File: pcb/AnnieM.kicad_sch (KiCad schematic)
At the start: 24 parts, among them J1 NRG200P, J2 NRG400, J3 SOLAR, U1 LMT86, U3 LM393

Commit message: added pull up to schematic
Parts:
- added R10: 100K, Resistor_SMD:R_0603_1608Metric, symbol Device:R
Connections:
- net VCC: now also R10.2
- net at C9.2, D1.1 (K), U3.1: now also R10.1
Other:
- moved on the sheet: D1
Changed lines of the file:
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@@
   (junction (at 156.21 82.55) (diameter 0) (color 0 0 0 0)
+  )
+  (junction (at 195.58 74.93) (diameter 0) (color 0 0 0 0)
   )
   (junction (at 133.35 109.22) (diameter 0) (color 0 0 0 0)
@@
     (stroke (width 0) (type default) (color 0 0 0 0))
   )
+  (wire (pts (xy 195.58 74.93) (xy 196.85 74.93))
+    (stroke (width 0) (type default) (color 0 0 0 0))
+  )
   (wire (pts (xy 149.86 74.93) (xy 156.21 74.93))
     (stroke (width 0) (type default) (color 0 0 0 0))
   )
-  (wire (pts (xy 199.39 74.93) (xy 201.93 74.93))
+  (wire (pts (xy 204.47 74.93) (xy 207.01 74.93))
     (stroke (width 0) (type default) (color 0 0 0 0))
   )
@@
     (stroke (width 0) (type default) (color 0 0 0 0))
   )
+  (wire (pts (xy 195.58 74.93) (xy 195.58 78.74))
+    (stroke (width 0) (type default) (color 0 0 0 0))
+  )
   (wire (pts (xy 146.05 36.83) (xy 154.94 36.83))
     (stroke (width 0) (type default) (color 0 0 0 0))
@@
     (stroke (width 0) (type default) (color 0 0 0 0))
   )
-  (wire (pts (xy 187.96 74.93) (xy 191.77 74.93))
+  (wire (pts (xy 187.96 74.93) (xy 195.58 74.93))
     (stroke (width 0) (type default) (color 0 0 0 0))
   )
@@
     )
   )
-  (global_label "SPEED" (shape output) (at 201.93 74.93 0) (fields_autoplaced)
+  (global_label "SPEED" (shape output) (at 207.01 74.93 0) (fields_autoplaced)
     (effects (font (size 1.27 1.27)) (justify left))
-    (property "Intersheet References" "${INTERSHEET_REFS}" (id 0) (at -11.43 29.21 0)
+    (property "Intersheet References" "${INTERSHEET_REFS}" (id 0) (at -6.35 29.21 0)
       (effects (font (size 1.27 1.27)) hide)
     )
@@
     )
     (property "Datasheet" "" (id 3) (at 240.03 69.85 0)
+      (effects (font (size 1.27 1.27)) hide)
+    )
+    (pin "1")
+  )
+  (symbol (lib_id "power:VCC") (at 195.58 86.36 180) (unit 1)
+    (in_bom yes) (on_board yes)
+    (property "Reference" "#PWR02" (id 0) (at 195.58 82.55 0)
+      (effects (font (size 1.27 1.27)) hide)
+    )
+    (property "Value" "VCC" (id 1) (at 195.58 91.44 0))
+    (property "Footprint" "" (id 2) (at 195.58 86.36 0)
+      (effects (font (size 1.27 1.27)) hide)
+    )
+    (property "Datasheet" "" (id 3) (at 195.58 86.36 0)
       (effects (font (size 1.27 1.27)) hide)
     )
@@
     (pin "1")
   )
-  (symbol (lib_id "Diode:1N914") (at 195.58 74.93 0) (unit 1)
+  (symbol (lib_id "Diode:1N914") (at 200.66 74.93 0) (unit 1)
     (in_bom yes) (on_board yes) (fields_autoplaced)
-    (property "Reference" "D1" (id 0) (at 195.58 68.58 0))
-    (property "Value" "1N914" (id 1) (at 195.58 71.12 0))
-    (property "Footprint" "Diode_THT:D_DO-35_SOD27_P7.62mm_Horizontal" (id 2) (at 195.58 79.375 0)
-      (effects (font (size 1.27 1.27)) hide)
-    )
-    (property "Datasheet" "http://www.vishay.com/docs/85622/1n914.pdf" (id 3) (at 195.58 74.93 0)
+    (property "Reference" "D1" (id 0) (at 200.66 68.58 0))
+    (property "Value" "1N914" (id 1) (at 200.66 71.12 0))
+    (property "Footprint" "Diode_THT:D_DO-35_SOD27_P7.62mm_Horizontal" (id 2) (at 200.66 79.375 0)
+      (effects (font (size 1.27 1.27)) hide)
+    )
+    (property "Datasheet" "http://www.vishay.com/docs/85622/1n914.pdf" (id 3) (at 200.66 74.93 0)
       (effects (font (size 1.27 1.27)) hide)
     )
@@
     )
     (pin "1")
+  )
+  (symbol (lib_id "Device:R") (at 195.58 82.55 0) (unit 1)
+    (in_bom yes) (on_board yes)
+    (property "Reference" "R10" (id 0) (at 193.04 82.55 90))
+    (property "Value" "100K" (id 1) (at 195.58 82.55 90))
+    (property "Footprint" "Resistor_SMD:R_0603_1608Metric" (id 2) (at 193.802 82.55 90)
+      (effects (font (size 1.27 1.27)) hide)
+    )
+    (property "Datasheet" "~" (id 3) (at 195.58 82.55 0)
+      (effects (font (size 1.27 1.27)) hide)
+    )
+    (pin "1")
+    (pin "2")
   )
   (symbol (lib_id "Device:C") (at 146.05 40.64 180) (unit 1)
@@
       (reference "#PWR01") (unit 1) (value "+10V") (footprint "")
     )
+    (path "/53498bcf-60b7-4c8d-9f37-8e4f9e563988"
+      (reference "#PWR02") (unit 1) (value "VCC") (footprint "")
+    )
     (path "/ba6c0b9c-fd1d-41af-a893-efc60d38ab3c"
       (reference "#PWR03") (unit 1) (value "+10V") (footprint "")
@@
       (reference "R9") (unit 1) (value "10K") (footprint "Resistor_SMD:R_0603_1608Metric")
     )
+    (path "/bbc3e4fe-b40f-4f24-b198-21d5f04f0ba7"
+      (reference "R10") (unit 1) (value "100K") (footprint "Resistor_SMD:R_0603_1608Metric")
+    )
     (path "/e0207eaa-3301-4772-a50e-fb4c3ab37719"

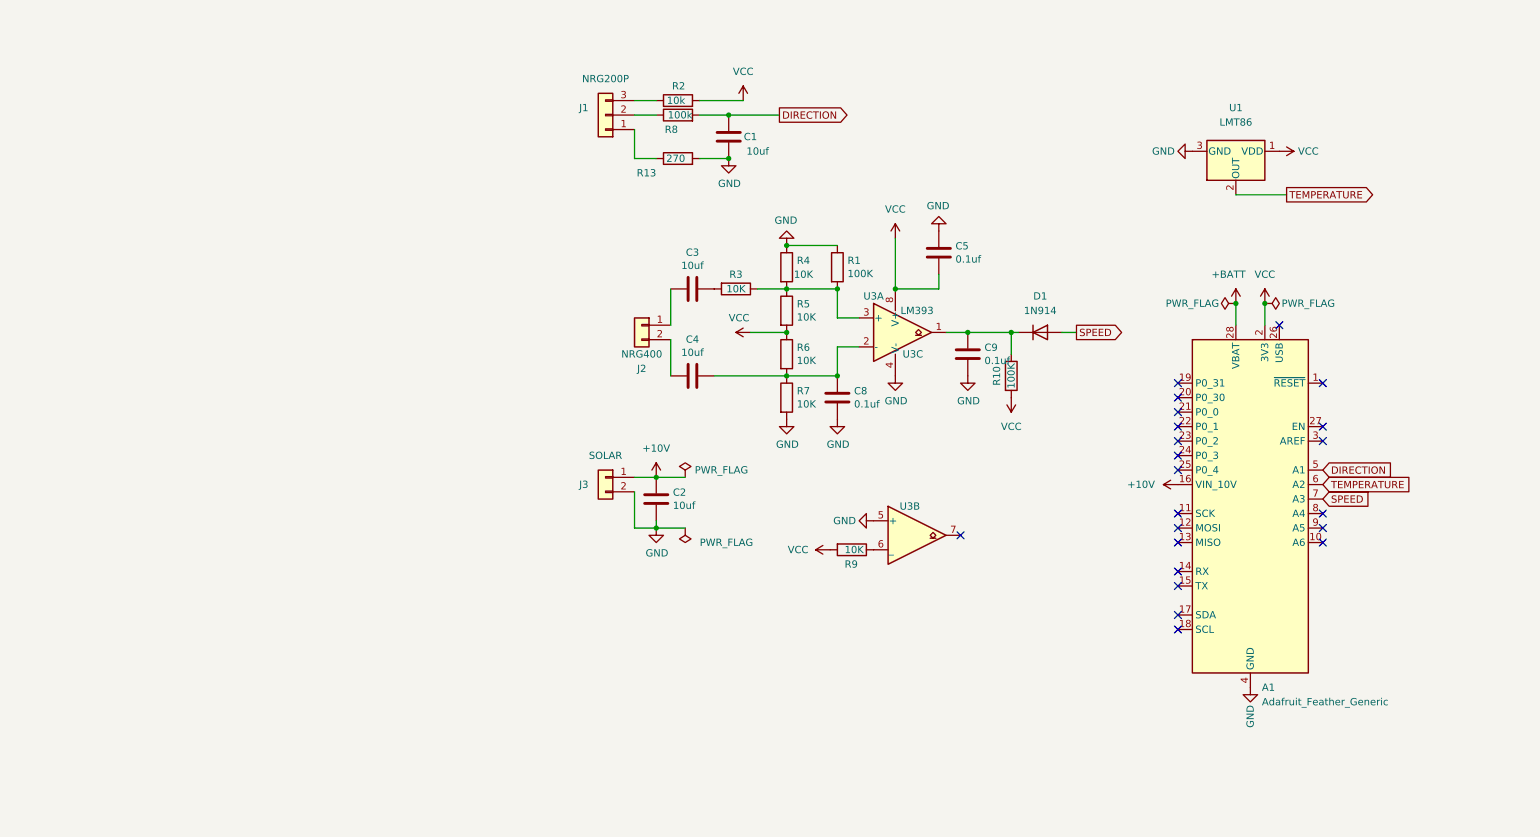
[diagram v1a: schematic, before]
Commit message: Restarted pcb layout, added bme866 and Arducam 5MP
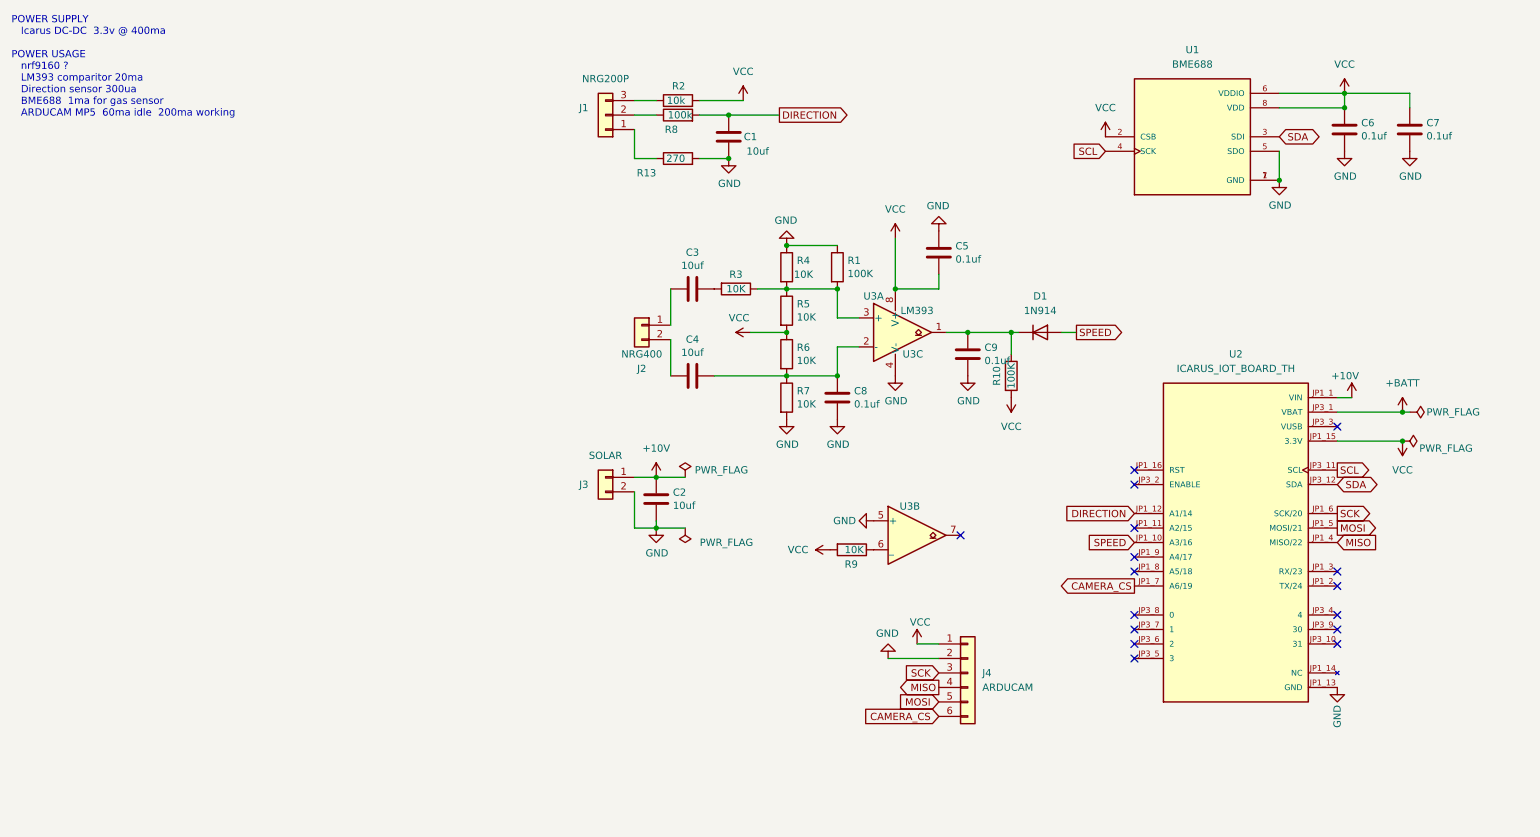
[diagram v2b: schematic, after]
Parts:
- removed A1: Adafruit_Feather_Generic, Module:Adafruit_Feather, symbol MCU_Module:Adafruit_Feather_Generic
- removed U1: LMT86, Package_TO_SOT_THT:TO-92_Inline, symbol Regulator_Linear:L78L18_TO92
- added C6, C7: 0.1uf, Capacitor_SMD:C_0603_1608Metric, symbol Device:C
- added J4: ARDUCAM, Connector_PinHeader_2.54mm:PinHeader_1x06_P2.54mm_Vertical, symbol Connector_Generic:Conn_01x06
- added U1: BME688, BME688:IC_BME688, symbol BME688:BME688
- added U2: ICARUS_IOT_BOARD_TH, ICARUS_IOT_BOARD_TH:MODULE_ICARUS_IOT_BOARD_TH, symbol ICARUS_IOT_BOARD_TH:ICARUS_IOT_BOARD_TH
- J1: footprint TerminalBlock_RND:TerminalBlock_RND_205-00288_1x03_P5.08mm_Horizontal -> TerminalBlock_RND:TerminalBlock_RND_205-00233_1x03_P5.08mm_Horizontal
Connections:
- net +10V: now also U2.JP1_1 (VIN)
- net +BATT: now also U2.JP3_1 (VBAT)
- net DIRECTION: now also U2.JP1_12 (A1/14)
- net GND: now also C6.1, C7.1, J4.2 (Pin_2), U1.1 (GND), U1.5 (SDO), U1.7 (GND), U2.JP1_13 (GND)
- net SPEED: now also U2.JP1_10 (A3/16)
- net VCC: now also C6.2, C7.2, J4.1 (Pin_1), U1.2 (CSB), U1.6 (VDDIO), U1.8 (VDD), U2.JP1_15 (3.3V)
- new net CAMERA_CS: J4.6 (Pin_6), U2.JP1_7 (A6/19)
- new net MISO: J4.4 (Pin_4), U2.JP1_4 (MISO/22)
- new net MOSI: J4.5 (Pin_5), U2.JP1_5 (MOSI/21)
- new net SCK: J4.3 (Pin_3), U2.JP1_6 (SCK/20)
- new net SCL: U1.4 (SCK), U2.JP3_11 (SCL)
- new net SDA: U1.3 (SDI), U2.JP3_12 (SDA)
- no-connect marks 22 -> 16
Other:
- note added: "POWER SUPPLY Icarus DC-DC 3.3v @ 400ma POWER USAGE nrf9160 ? LM393 comparitor 20ma Direction sensor 300ua BME688 1ma for gas sensor ARDUCAM MP5 60ma idle 200ma working"

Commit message: relayout, new temp and camera connection
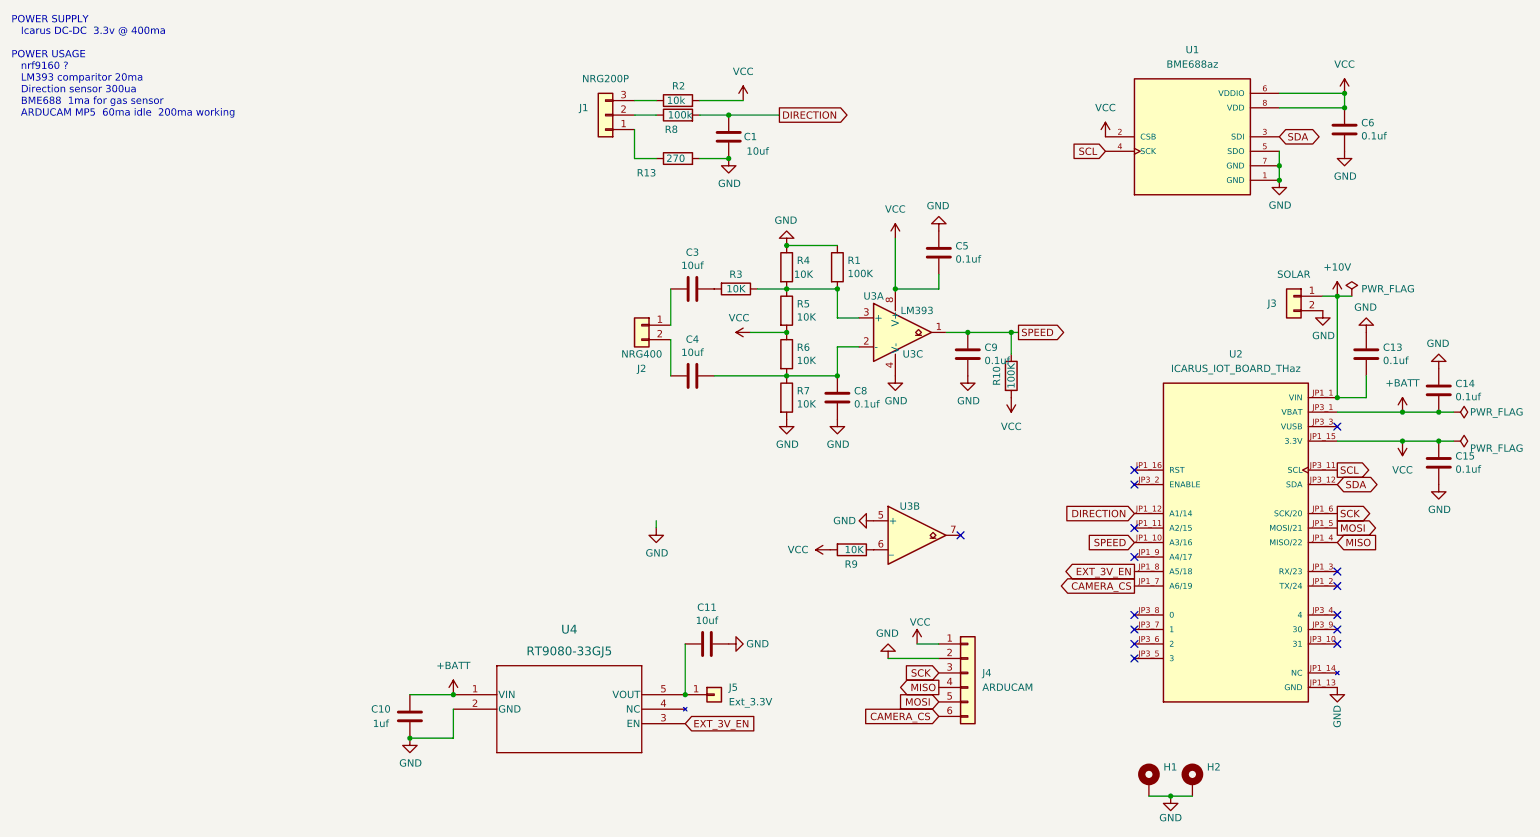
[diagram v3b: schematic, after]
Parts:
- removed C2: 10uf, Capacitor_SMD:C_0805_2012Metric, symbol Device:C
- removed C7: 0.1uf, Capacitor_SMD:C_0603_1608Metric, symbol Device:C
- removed D1: 1N914, Diode_THT:D_DO-35_SOD27_P7.62mm_Horizontal, symbol Diode:1N914
- removed U1: BME688, BME688:IC_BME688, symbol BME688:BME688
- removed U2: ICARUS_IOT_BOARD_TH, ICARUS_IOT_BOARD_TH:MODULE_ICARUS_IOT_BOARD_TH, symbol ICARUS_IOT_BOARD_TH:ICARUS_IOT_BOARD_TH
- added C10: 1uf, Capacitor_SMD:C_0805_2012Metric, symbol Device:C
- added C11: 10uf, Capacitor_SMD:C_0805_2012Metric, symbol Device:C
- added C13, C14, C15: 0.1uf, Capacitor_SMD:C_0603_1608Metric, symbol Device:C
- added H1, H2: (no value), MountingHole:MountingHole_2.2mm_M2_DIN965_Pad, symbol Mechanical:MountingHole_Pad
- added J5: Ext_3.3V, Connector_PinSocket_2.54mm:PinSocket_1x01_P2.54mm_Vertical, symbol Connector_Generic:Conn_01x01
- added U1: BME688az, BME688:IC_BME688, symbol BME688:BME688az
- added U2: ICARUS_IOT_BOARD_THaz, ICARUS_IOT_BOARD_TH:MODULE_ICARUS_IOT_BOARD_THaz, symbol ICARUS_IOT_BOARD_TH:ICARUS_IOT_BOARD_THaz
- added U4: RT9080-33GJ5, Package_TO_SOT_SMD:TSOT-23-5, symbol 2023-12-11_22-26-01:RT9080-33GJ5
- J3: footprint Connector_PinSocket_2.54mm:PinSocket_1x02_P2.54mm_Vertical -> Connector_JST:JST_XA_B02B-XASK-1_1x02_P2.50mm_Vertical
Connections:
- net +10V: now also C13.1, U2.JP1_1 (VIN)
- net +BATT: now also C10.1, C14.1, U2.JP3_1 (VBAT), U4.1 (VIN)
- net CAMERA_CS: now also U2.JP1_7 (A6/19)
- net DIRECTION: now also U2.JP1_12 (A1/14)
- net GND: now also C10.2, C11.1, C13.2, C14.2, C15.1, H1.1, H2.1, U1.1 (GND), U1.5 (SDO), U1.7 (GND), U2.JP1_13 (GND), U4.2 (GND)
- net MISO: now also U2.JP1_4 (MISO/22)
- net MOSI: now also U2.JP1_5 (MOSI/21)
- net SCK: now also U2.JP1_6 (SCK/20)
- net SCL: now also U1.4 (SCK), U2.JP3_11 (SCL)
- net SDA: now also U1.3 (SDI), U2.JP3_12 (SDA)
- net SPEED: now also C9.2, R10.1, U3.1, U2.JP1_10 (A3/16)
- net VCC: now also C15.2, U1.2 (CSB), U1.6 (VDDIO), U1.8 (VDD), U2.JP1_15 (3.3V)
- new net: C11.2, J5.1 (Pin_1), U4.5 (VOUT)
- new net EXT_3V_EN: U2.JP1_8 (A5/18), U4.3 (EN)
- no-connect marks 16 -> 15
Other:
- moved on the sheet: J3

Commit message: Reordered annotations graphically
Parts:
- H1, H2: now left out of the parts list
- renumbered C15 to C1, C6 to C10, C10 to C12, C1 to C2, C14 to C3, C3 to C4, C4 to C5, C9 to C6, C8 to C7, C5 to C8, C13 to C9, J2 to J1, J1 to J2, R2 to R1, R9 to R11, R8 to R2, R13 to R3, R3 to R4, R4 to R7, R7 to R8, R1 to R9, U3 to U1, U1 to U2, U2 to U3

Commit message: Minor changes, Sent off to OSHPark
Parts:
- added J6: EXT_BME280, Connector_PinSocket_2.54mm:PinSocket_1x04_P2.54mm_Vertical, symbol Connector_Generic:Conn_01x04
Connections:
- net GND: now also J6.1 (Pin_1)
- net VCC: now also J6.2 (Pin_2)
- net SDA_EX: now reaches U3.JP3_4 (4)
- net SDA_EX: now also J6.3 (Pin_3)
- net SCL_EX: now reaches U3.JP3_5 (3)
- net SCL_EX: now also J6.4 (Pin_4)
- no-connect marks 15 -> 13
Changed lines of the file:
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@@
   (no_connect (at 217.17 114.3))
   (no_connect (at 217.17 124.46))
-  (no_connect (at 217.17 132.08))
   (no_connect (at 217.17 129.54))
   (no_connect (at 217.17 127))
@@
   (no_connect (at 252.73 129.54))
   (no_connect (at 252.73 127))
-  (no_connect (at 252.73 124.46))
   (no_connect (at 217.17 99.06))
   (no_connect (at 217.17 101.6))
@@
     )
   )
+  (global_label "SCL_EX" (shape input) (at 182.88 156.21 180) (fields_autoplaced)
+    (effects (font (size 1.27 1.27)) (justify right))
+    (property "Intersheet References" "${INTERSHEET_REFS}" (id 0) (at 173.722 156.1306 0)
+      (effects (font (size 1.27 1.27)) (justify right) hide)
+    )
+  )
   (global_label "CAMERA_CS" (shape input) (at 182.88 142.24 180) (fields_autoplaced)
     (effects (font (size 1.27 1.27)) (justify right))
@@
     )
   )
+  (global_label "SDA_EX" (shape bidirectional) (at 217.17 134.62 180) (fields_autoplaced)
+    (effects (font (size 1.27 1.27)) (justify right))
+    (property "Intersheet References" "${INTERSHEET_REFS}" (id 0) (at 207.9515 134.5406 0)
+      (effects (font (size 1.27 1.27)) (justify right) hide)
+    )
+  )
   (global_label "MOSI" (shape output) (at 252.73 109.22 0) (fields_autoplaced)
     (effects (font (size 1.27 1.27)) (justify left))
@@
     (property "Intersheet References" "${INTERSHEET_REFS}" (id 0) (at 258.6223 101.5206 0)
       (effects (font (size 1.27 1.27)) (justify left) hide)
+    )
+  )
+  (global_label "SDA_EX" (shape bidirectional) (at 182.88 153.67 180) (fields_autoplaced)
+    (effects (font (size 1.27 1.27)) (justify right))
+    (property "Intersheet References" "${INTERSHEET_REFS}" (id 0) (at 173.6615 153.5906 0)
+      (effects (font (size 1.27 1.27)) (justify right) hide)
+    )
+  )
+  (global_label "SCL_EX" (shape output) (at 217.17 132.08 180) (fields_autoplaced)
+    (effects (font (size 1.27 1.27)) (justify right))
+    (property "Intersheet References" "${INTERSHEET_REFS}" (id 0) (at 208.012 132.0006 0)
+      (effects (font (size 1.27 1.27)) (justify right) hide)
     )
   )
@@
     )
     (property "Datasheet" "" (id 3) (at 212.09 40.64 0)
+      (effects (font (size 1.27 1.27)) hide)
+    )
+    (pin "1")
+  )
+  (symbol (lib_id "power:GND") (at 182.88 148.59 270) (unit 1)
+    (in_bom yes) (on_board yes)
+    (property "Reference" "#PWR022" (id 0) (at 176.53 148.59 0)
+      (effects (font (size 1.27 1.27)) hide)
+    )
+    (property "Value" "GND" (id 1) (at 178.4858 148.717 90))
+    (property "Footprint" "" (id 2) (at 182.88 148.59 0)
+      (effects (font (size 1.27 1.27)) hide)
+    )
+    (property "Datasheet" "" (id 3) (at 182.88 148.59 0)
       (effects (font (size 1.27 1.27)) hide)
     )
@@
     (pin "1")
   )
+  (symbol (lib_id "Connector_Generic:Conn_01x04") (at 187.96 151.13 0) (unit 1)
+    (in_bom yes) (on_board yes) (fields_autoplaced)
+    (property "Reference" "J6" (id 0) (at 190.5 151.1299 0)
+      (effects (font (size 1.27 1.27)) (justify left))
+    )
+    (property "Value" "EXT_BME280" (id 1) (at 190.5 153.6699 0)
+      (effects (font (size 1.27 1.27)) (justify left))
+    )
+    (property "Footprint" "Connector_PinSocket_2.54mm:PinSocket_1x04_P2.54mm_Vertical" (id 2) (at 187.96 151.13 0)
+      (effects (font (size 1.27 1.27)) hide)
+    )
+    (property "Datasheet" "~" (id 3) (at 187.96 151.13 0)
+      (effects (font (size 1.27 1.27)) hide)
+    )
+    (pin "1")
+    (pin "2")
+    (pin "3")
+    (pin "4")
+  )
+  (symbol (lib_id "power:VCC") (at 182.88 151.13 90) (unit 1)
+    (in_bom yes) (on_board yes)
+    (property "Reference" "#PWR026" (id 0) (at 186.69 151.13 0)
+      (effects (font (size 1.27 1.27)) hide)
+    )
+    (property "Value" "VCC" (id 1) (at 179.07 151.13 90)
+      (effects (font (size 1.27 1.27)) (justify left))
+    )
+    (property "Footprint" "" (id 2) (at 182.88 151.13 0)
+      (effects (font (size 1.27 1.27)) hide)
+    )
+    (property "Datasheet" "" (id 3) (at 182.88 151.13 0)
+      (effects (font (size 1.27 1.27)) hide)
+    )
+    (pin "1")
+  )
   (symbol (lib_id "Device:R") (at 195.58 82.55 0) (unit 1)
     (in_bom yes) (on_board yes)
@@
       (reference "#PWR021") (unit 1) (value "GND") (footprint "")
     )
+    (path "/2c9f314d-5a8a-480b-a11e-8dd624a919f2"
+      (reference "#PWR022") (unit 1) (value "GND") (footprint "")
+    )
     (path "/d1b10d5e-568e-4308-b1f2-a6ce889b69cf"
       (reference "#PWR023") (unit 1) (value "GND") (footprint "")
@@
       (reference "#PWR025") (unit 1) (value "GND") (footprint "")
     )
+    (path "/bb7c3a65-1995-4497-8297-8ca2fbc117bf"
+      (reference "#PWR026") (unit 1) (value "VCC") (footprint "")
+    )
     (path "/00000000-0000-0000-0000-000062daef7a"
       (reference "#PWR0101") (unit 1) (value "GND") (footprint "")
@@
       (reference "J5") (unit 1) (value "Ext_3.3V") (footprint "Connector_PinSocket_2.54mm:PinSocket_1x01_P2.54mm_Vertical")
     )
+    (path "/b6e90fef-7cd6-4993-b736-f3c66b5e8308"
+      (reference "J6") (unit 1) (value "EXT_BME280") (footprint "Connector_PinSocket_2.54mm:PinSocket_1x04_P2.54mm_Vertical")
+    )
     (path "/c9b1f32c-bc96-4ee4-9069-c41b35fa9dce"
